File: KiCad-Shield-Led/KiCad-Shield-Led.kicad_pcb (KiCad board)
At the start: 2 copper layers, 68.6 x 53.3 mm, 8 parts, among them P1 Power, P2 Analog, P3 Digital, P4 Digital, P5 CONN_01X01, P6 CONN_01X01, P7 CONN_01X01, P8 CONN_01X01

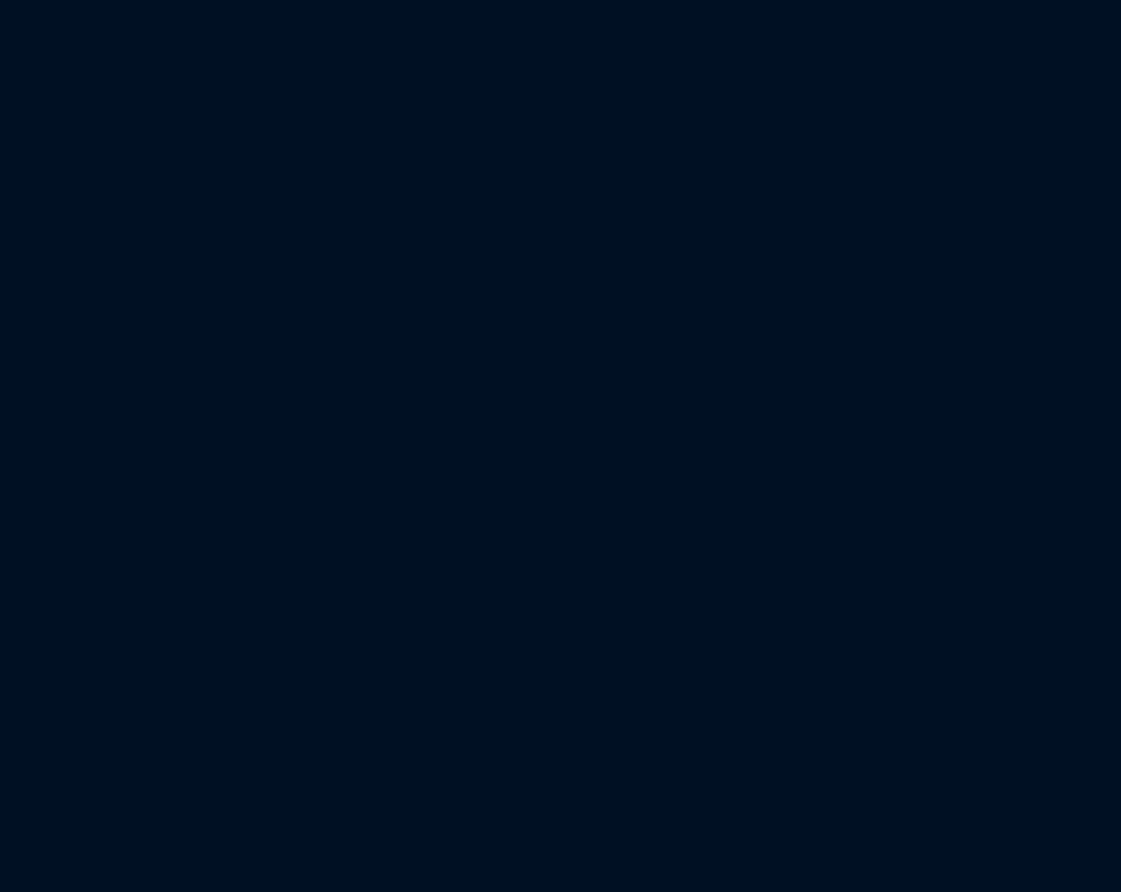
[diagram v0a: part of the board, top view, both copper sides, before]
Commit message: Add class Equipot for routine
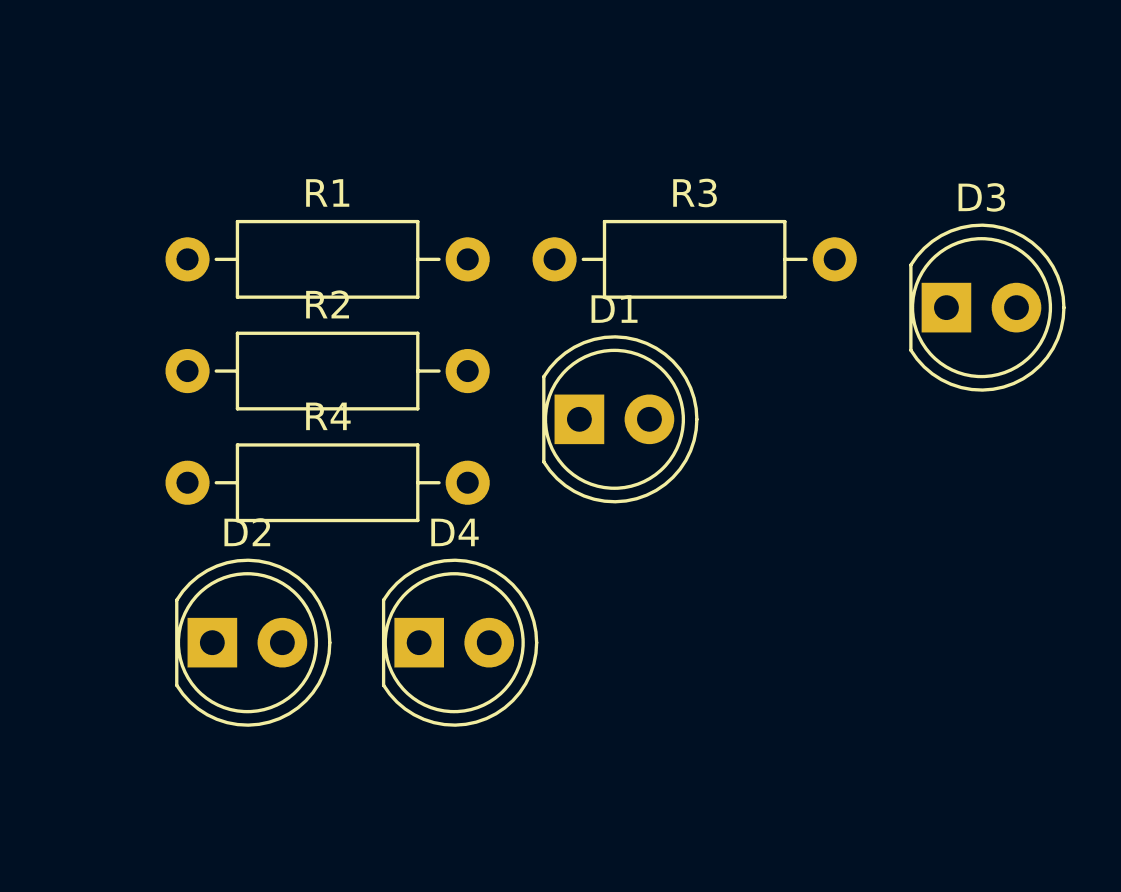
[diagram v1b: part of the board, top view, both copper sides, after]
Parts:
- added D1: LED, LED_THT:LED_D5.0mm, F.Cu at (201.2, 101.9)
- added D2: LED, LED_THT:LED_D5.0mm, F.Cu at (187.9, 110.0)
- added D3: LED, LED_THT:LED_D5.0mm, F.Cu at (214.5, 97.9)
- added D4: LED, LED_THT:LED_D5.0mm, F.Cu at (195.4, 110.0)
- added R1: 470, Resistor_THT:R_Axial_DIN0207_L6.3mm_D2.5mm_P10.16mm_Horizontal, F.Cu at (187.0, 96.1)
- added R2: 470, Resistor_THT:R_Axial_DIN0207_L6.3mm_D2.5mm_P10.16mm_Horizontal, F.Cu at (187.0, 100.2)
- added R3: 470, Resistor_THT:R_Axial_DIN0207_L6.3mm_D2.5mm_P10.16mm_Horizontal, F.Cu at (200.3, 96.1)
- added R4: 470, Resistor_THT:R_Axial_DIN0207_L6.3mm_D2.5mm_P10.16mm_Horizontal, F.Cu at (187.0, 104.2)
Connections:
- P3 pad 6: /12(MISO) -> /LED1
- P3 pad 7: /11(**/MOSI) -> /LED2
- P3 pad 8: /10(**/SS) -> /LED3
- P3 pad 9: /9(**) -> /LED4
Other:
- net class Default: clearance 0.2 -> 0.8; trace_width 0.25 -> 0.8; via_dia 0.6 -> 1.2; via_drill 0.4 -> 0.8
- net class Power added: clearance 0.8, trace_width 1.2, via_dia 1.2, via_drill 0.8
- rule trace_clearance: 0.2 -> 0.8
- rule trace_min: 0.2 -> 0
- rule via_min_drill: 0.3 -> 0
- rule via_min_size: 0.4 -> 0
